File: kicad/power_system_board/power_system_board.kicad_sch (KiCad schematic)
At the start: 0 parts

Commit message: Idea for how we could do charging
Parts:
- added BT1, BT2: Battery_Cell, symbol Device:Battery_Cell
- added C1, C2, C3, C4: 4.7u, symbol Device:C
- added D1, D2: LED, symbol Device:LED
- added J1: USB_B_Micro, symbol Connector:USB_B_Micro
- added R1, R2: 0, symbol Device:R
- added R3, R6: 2k, symbol Device:R
- added R4, R5: 470, symbol Device:R
- added U1, U2: MCP73831-2-OT, Package_TO_SOT_SMD:SOT-23-5, symbol Battery_Management:MCP73831-2-OT
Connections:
- new net: BT2.2 (-), R1.1
- new net: R6.1, U2.5 (PROG)
- new net: BT1.1 (+), R2.2
- new net: R4.1, U1.1 (STAT)
- new net: R3.1, U1.5 (PROG)
- new net: D1.1 (K), R4.2
- new net: R5.1, U2.1 (STAT)
- new net: D2.1 (K), R5.2
- new net +BATT: C1.1, R2.1, U1.3 (V_{BAT})
- new net -BATT: C3.1, C4.2, R1.2, R6.2, U2.2 (V_{SS})
- new net GND: J1.5 (GND)
- new net MID_BATT: BT1.2 (-), BT2.1 (+), C1.2, C2.1, C4.1, R3.2, U1.2 (V_{SS}), U2.3 (V_{BAT})
- new net VBUS: C2.2, C3.2, D1.2 (A), D2.2 (A), J1.1 (VBUS), U1.4 (V_{DD}), U2.4 (V_{DD})
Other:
- note added: "TODO: 1. Battery Charger IC (MCP73831/2 or TP______ something) 2. Undervoltage Lockout 3. Polarity Protection 4. Regulated power rails (5V, 3V3, ..?) 5. Battery health circuit 6. Section for USB input"
- note removed: "TODO: 1. Battery Charger IC (MCP73831/2 or TP______ something) 2. Undervoltage Lockout 3. Polarity Protection 4. Regulated power rails (5V, 3V3, ..?) 5. Battery health circuit"

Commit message: Big headway on the power module
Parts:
- removed R5: 470, symbol Device:R
- removed R6: 2k, symbol Device:R
- C1, C2, C3, C4: footprint (none) -> Capacitor_SMD:C_0805_2012Metric
- D1, D2: footprint (none) -> LED_SMD:LED_0805_2012Metric
- R1: value 0 -> 470; footprint (none) -> Resistor_SMD:R_0805_2012Metric
- R2: value 0 -> 2k
- R4: footprint (none) -> Resistor_SMD:R_0805_2012Metric
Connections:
- net VBUS: now also C2.1, C3.1; no longer C2.2, C3.2
- net at R1.1: now also U2.1 (STAT); no longer BT2.2 (-)
- net at U2.5 (PROG): now also R2.1
- net +BATT1: now reaches BT1.1 (+)
- net +BATT1: now also C1.1, U1.3 (V_{BAT}); no longer R2.2
- net at D2.1 (K): now also R1.2
- removed net +BATT: C1.1, R2.1, U1.3 (V_{BAT})
- net -BATT renamed -BATT2
- net -BATT2: now also BT2.2 (-), C3.2, R2.2; no longer C3.1, R1.2
- net MID_BATT renamed -BATT1
- net -BATT1: now also C2.2; no longer BT2.1 (+), C2.1, C4.1, U2.3 (V_{BAT})
- new net +BATT2: BT2.1 (+), C4.1, U2.3 (V_{BAT})
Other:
- note added: "TODO: (done in brackets) (1.) Battery Charger IC (MCP73831/2 or TP______ something) 2. Undervoltage Lockout 3. Polarity Protection 4. Regulated power rails (5V, 3V3, ..?) 5. Battery health circuit 6. Section for USB input 7. Inline fuse rated at 150% the current of each battery"
- note added: "Unprotected Cells 18650 Cells for now V rated at 3.7V I rated at ????"
- note removed: "TODO: 1. Battery Charger IC (MCP73831/2 or TP______ something) 2. Undervoltage Lockout 3. Polarity Protection 4. Regulated power rails (5V, 3V3, ..?) 5. Battery health circuit 6. Section for USB input"
- moved on the sheet: BT1, C1, D1, J1, R3, R4, U1

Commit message: Its impossible with 2 cells
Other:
- note added: "TODO: (done in brackets) (1.) Battery Charger IC (MCP73831/2 or TP______ something) 2. Undervoltage Lockout 3. Polarity Protection 4. Regulated power rails (JUST 5V) 5. Battery health circuit 6. Section for USB input 7. Inline fuse rated at 150% the current of each battery"
- note removed: "TODO: (done in brackets) (1.) Battery Charger IC (MCP73831/2 or TP______ something) 2. Undervoltage Lockout 3. Polarity Protection 4. Regulated power rails (5V, 3V3, ..?) 5. Battery health circuit 6. Section for USB input 7. Inline fuse rated at 150% the current of each battery"
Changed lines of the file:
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@@
 		)
 	)
-	(text "TODO: (done in brackets)\n(1.) Battery Charger IC (MCP73831/2 or TP______ something)\n2. Undervoltage Lockout\n3. Polarity Protection\n4. Regulated power rails (5V, 3V3, ..?)\n5. Battery health circuit\n6. Section for USB input\n7. Inline fuse rated at 150% the current of each battery\n"
+	(text "TODO: (done in brackets)\n(1.) Battery Charger IC (MCP73831/2 or TP______ something)\n2. Undervoltage Lockout\n3. Polarity Protection\n4. Regulated power rails (JUST 5V)\n5. Battery health circuit\n6. Section for USB input\n7. Inline fuse rated at 150% the current of each battery\n"
 		(exclude_from_sim no)
 		(at 102.362 29.972 0)

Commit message: Nearing end of design
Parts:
- removed BT2: Battery_Cell, symbol Device:Battery_Cell
- removed C4: 4.7u, Capacitor_SMD:C_0805_2012Metric, symbol Device:C
- removed D2: LED, LED_SMD:LED_0805_2012Metric, symbol Device:LED
- removed U2: MCP73831-2-OT, Package_TO_SOT_SMD:SOT-23-5, symbol Battery_Management:MCP73831-2-OT
- added Q1, Q2: 2N7002H, Package_TO_SOT_SMD:SOT-23, symbol Transistor_FET:2N7002H
- added U2: AP9101CK, Package_TO_SOT_SMD:SOT-23-5, symbol Battery_Management:AP9101CK
- C3: value 4.7u -> 100n
- R1: value 470 -> 2k7
- R2: value 2k -> 330; footprint (none) -> Resistor_SMD:R_0805_2012Metric
- R3: footprint (none) -> Resistor_SMD:R_0805_2012Metric
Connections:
- net GND: now also C1.2, C2.2, R1.1, R3.2, U1.2 (V_{SS})
- net VBUS: no longer C3.1
- net at R1.2: now also U2.1 (VM)
- net at R2.1: now also C3.2, U2.2 (VDD)
- net +BATT1 renamed +BATT
- net +BATT: now also R2.2, Q2.2 (S)
- removed net -BATT1: BT1.2 (-), C1.2, C2.2, R3.2, U1.2 (V_{SS})
- removed net -BATT2: C3.2, R2.2
- new net: Q1.1 (G), U2.4 (DO)
- new net: Q1.3 (D), Q2.3 (D)
- new net: Q2.1 (G), U2.5 (CO)
- new net -BATT: BT1.2 (-), C3.1, Q1.2 (S), U2.3 (VSS)
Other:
- note added: "TODO: (done in brackets) (1.) Battery Charger IC (MCP73831/2 or TP______ something) 2. Undervoltage Lockout 3. Polarity Protection 4. Regulated power rails (3V3 - Done on perf board, not on PCB) 5. Battery health circuit 6. Section for USB input 7. Inline fuse rated at 150% the current of each battery"
- note removed: "TODO: (done in brackets) (1.) Battery Charger IC (MCP73831/2 or TP______ something) 2. Undervoltage Lockout 3. Polarity Protection 4. Regulated power rails (JUST 5V) 5. Battery health circuit 6. Section for USB input 7. Inline fuse rated at 150% the current of each battery"
- note removed: "Unprotected Cells 18650 Cells for now V rated at 3.7V I rated at ????"
- moved on the sheet: BT1

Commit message: Checkpoint
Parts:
- removed U2: AP9101CK, Package_TO_SOT_SMD:SOT-23-5, symbol Battery_Management:AP9101CK
- added J2: Conn_01x04_Pin, Connector_PinHeader_2.54mm:PinHeader_1x04_P2.54mm_Vertical, symbol Connector:Conn_01x04_Pin
- added J3, J4, J5, J6: Conn_01x02_Pin, Connector_PinHeader_2.54mm:PinHeader_1x02_P2.54mm_Vertical, symbol Connector:Conn_01x02_Pin
- added R5: 330m, Resistor_SMD:R_0805_2012Metric, symbol Device:R
- added U3: AP9101CK6, Package_TO_SOT_SMD:SOT-23-6, symbol Battery_Management:AP9101CK6
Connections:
- net +BATT: now also J4.1 (Pin_1), J5.2 (Pin_2); no longer BT1.1 (+)
- net -BATT: now also J3.2 (Pin_2), R5.2, U3.6 (VSS); no longer BT1.2 (-), Q1.2 (S)
- net VBUS: now also J2.4 (Pin_4)
- net at J1.2 (D-): now also J2.2 (Pin_2)
- net at J1.3 (D+): now also J2.3 (Pin_3)
- net at J1.4 (ID): now also J2.1 (Pin_1)
- net at Q1.1 (G): now also U3.1 (DO)
- net at Q1.3 (D), Q2.3 (D): now also J5.1 (Pin_1), J6.2 (Pin_2)
- net at Q2.1 (G): now also U3.3 (CO)
- net at R1.2: now also U3.2 (VM)
- net at C3.2, R2.1: now also U3.5 (VDD)
- new net: BT1.1 (+), J4.2 (Pin_2)
- new net: BT1.2 (-), J3.1 (Pin_1)
- new net: J6.1 (Pin_1), Q1.2 (S), R5.1
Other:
- moved on the sheet: BT1, C3, Q1, Q2, R1, R2

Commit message: Checkpoint
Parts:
- added J7: Conn_01x02_Pin, Connector_PinHeader_2.54mm:PinHeader_1x02_P2.54mm_Vertical, symbol Connector:Conn_01x02_Pin
- U3: value AP9101CK6 -> AP9101CK6-AYTRG1
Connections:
- net GND: now also J7.1 (Pin_1)
- net at BT1.2 (-), J3.1 (Pin_1): now also J7.2 (Pin_2)
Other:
- note added: "TODO: (done in brackets) (1.) Battery Charger IC (MCP73831/2 or TP______ something) (2.) Undervoltage Lockout 3. Polarity Protection 4. Regulated power rails (3V3 - Done on perf board, not on PCB) 5. Battery health circuit 6. Section for USB input 7. Inline fuse rated at 150% the current of each battery"
- note removed: "TODO: (done in brackets) (1.) Battery Charger IC (MCP73831/2 or TP______ something) 2. Undervoltage Lockout 3. Polarity Protection 4. Regulated power rails (3V3 - Done on perf board, not on PCB) 5. Battery health circuit 6. Section for USB input 7. Inline fuse rated at 150% the current of each battery"
- moved on the sheet: BT1, J1, J2, J3, J4

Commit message: Need to add esp32 and fix USB
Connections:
- net +BATT: no longer J5.2 (Pin_2), Q2.2 (S)
- net -BATT: now also J6.1 (Pin_1)
- net GND: now also J5.2 (Pin_2), Q2.2 (S)
- net at Q1.2 (S), R5.1: no longer J6.1 (Pin_1)
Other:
- note added: "TODO: (done in brackets) (1.) Battery Charger IC (MCP73831/2 or TP______ something) (2.) Undervoltage Lockout (3.) Polarity Protection (4.) Regulated power rails (3V3 - Done on perf board, not on PCB) 5. Battery health circuit 6. Section for USB input 7. Inline fuse rated at 150% the current of each battery"
- note removed: "TODO: (done in brackets) (1.) Battery Charger IC (MCP73831/2 or TP______ something) (2.) Undervoltage Lockout 3. Polarity Protection 4. Regulated power rails (3V3 - Done on perf board, not on PCB) 5. Battery health circuit 6. Section for USB input 7. Inline fuse rated at 150% the current of each battery"
- moved on the sheet: R5
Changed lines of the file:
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@@
 		(rev "0")
 		(company "University of Cape Town")
-		(comment 1 "Designer: Harry Papanicolaou")
+		(comment 1 "Harry Papanicolaou")
+		(comment 2 "Designers: Adrian McIntosh")
 	)
 	(junction
@@
 	)
 	(junction
-		(at 121.92 62.23)
-		(diameter 0)
-		(color 0 0 0 0)
-	)
-	(junction
 		(at 133.35 77.47)
 		(diameter 0)
@@
 	)
 	(junction
-		(at 133.35 62.23)
+		(at 33.02 35.56)
 		(diameter 0)
 		(color 0 0 0 0)
 	)
 	(junction
-		(at 33.02 35.56)
+		(at 45.72 62.23)
 		(diameter 0)
 		(color 0 0 0 0)
 	)
 	(junction
-		(at 45.72 62.23)
+		(at 83.82 22.86)
 		(diameter 0)
 		(color 0 0 0 0)
 	)
 	(junction
-		(at 63.5 67.31)
+		(at 147.32 91.44)
 		(diameter 0)
 		(color 0 0 0 0)
 	)
 	(junction
-		(at 83.82 22.86)
+		(at 63.5 67.31)
 		(diameter 0)
 		(color 0 0 0 0)
 	)
 	(junction
-		(at 45.72 82.55)
+		(at 133.35 62.23)
 		(diameter 0)
 		(color 0 0 0 0)
 	)
 	(junction
-		(at 133.35 90.17)
+		(at 45.72 82.55)
 		(diameter 0)
 		(color 0 0 0 0)
@@
 	(wire
 		(pts
-			(xy 133.35 88.9) (xy 133.35 90.17)
+			(xy 133.35 88.9) (xy 133.35 91.44)
 		)
 		(stroke
@@
 	(wire
 		(pts
-			(xy 143.51 95.25) (xy 147.32 95.25)
+			(xy 143.51 91.44) (xy 147.32 91.44)
 		)
 		(stroke
@@
 	(wire
 		(pts
-			(xy 133.35 90.17) (xy 133.35 95.25)
+			(xy 133.35 74.93) (xy 133.35 77.47)
 		)
 		(stroke
@@
 	(wire
 		(pts
-			(xy 133.35 74.93) (xy 133.35 77.47)
+			(xy 45.72 60.96) (xy 45.72 62.23)
 		)
 		(stroke
@@
 	(wire
 		(pts
-			(xy 45.72 60.96) (xy 45.72 62.23)
+			(xy 127 58.42) (xy 127 59.69)
 		)
 		(stroke
@@
 	(wire
 		(pts
-			(xy 147.32 86.36) (xy 147.32 90.17)
+			(xy 147.32 86.36) (xy 147.32 91.44)
 		)
 		(stroke
@@
 	(wire
 		(pts
+			(xy 147.32 91.44) (xy 147.32 95.25)
+		)
+		(stroke
+			(width 0)
+			(type default)
+		)
+	)
+	(wire
+		(pts
 			(xy 147.32 72.39) (xy 147.32 77.47)
 		)
@@
 	(wire
 		(pts
-			(xy 133.35 62.23) (xy 121.92 62.23)
-		)
-		(stroke
-			(width 0)
-			(type default)
-		)
-	)
-	(wire
-		(pts
 			(xy 21.59 38.1) (xy 29.21 38.1)
 		)
@@
 	(wire
 		(pts
-			(xy 133.35 95.25) (xy 135.89 95.25)
+			(xy 133.35 91.44) (xy 135.89 91.44)
 		)
 		(stroke
@@
 	(wire
 		(pts
-			(xy 147.32 90.17) (xy 133.35 90.17)
+			(xy 63.5 67.31) (xy 63.5 69.85)
 		)
 		(stroke
@@
 	(wire
 		(pts
-			(xy 63.5 67.31) (xy 63.5 69.85)
+			(xy 133.35 58.42) (xy 127 58.42)
 		)
 		(stroke
@@
 	(wire
 		(pts
+			(xy 133.35 62.23) (xy 133.35 58.42)
+		)
+		(stroke
+			(width 0)
+			(type default)
+		)
+	)
+	(wire
+		(pts
 			(xy 115.57 80.01) (xy 120.65 80.01)
 		)
@@
 	(rectangle
 		(start 77.47 52.07)
-		(end 179.07 125.73)
+		(end 173.99 125.73)
 		(stroke
 			(width 0)
@@
 	(rectangle
 		(start 12.7 52.07)
-		(end 76.2 125.73)
+		(end 76.2 116.84)
 		(stroke
 			(width 0)
@@
 	)
 	(image
-		(at 33.02 106.68)
+		(at 33.02 104.14)
 		(scale 0.158222)
 		(data "iVBORw0KGgoAAAANSUhEUgAAA3sAAAIfCAYAAADJ38UbAAAAAXNSR0IArs4c6QAAAARnQU1BAACx"
@@
 		)
 	)
-	(text_box "AP9101C\n1) Protects from overdischarge (UVLO)\n2) Selectable power-down mode. We don't need this\n\n<< This is a reference, but because of the charging circuit, P- and GND are swapped\nI saw a video on youtube saying that a small resister where R5 is would make it smoother"
+	(text_box "AP9101C battery protection circuit with failsafes\n1) Protects from overdischarge (UVLO)\n2) Selectable power-down mode. We don't need this\n3) Overdischarge also works as polarity protection :)\n\n<< This is a reference, but because of the charging circuit, P- and GND are swapped\nI saw a video on youtube saying that a small resister where R5 is would make it smoother"
 		(exclude_from_sim no)
 		(at 116.84 101.6 0)
-		(size 44.45 21.59)
+		(size 55.88 22.86)
 		(stroke
 			(width 0)
@@
 	(text_box "Battery Charging IC modules\nEach cell is disconnected and charged seperately from one another"
 		(exclude_from_sim no)
-		(at 52.07 100.33 0)
+		(at 52.07 97.79 0)
 		(size 22.86 17.78)
 		(stroke
@@
 		)
 	)
-	(text "TODO: (done in brackets)\n(1.) Battery Charger IC (MCP73831/2 or TP______ something)\n(2.) Undervoltage Lockout\n3. Polarity Protection\n4. Regulated power rails (3V3 - Done on perf board, not on PCB)\n5. Battery health circuit\n6. Section for USB input\n7. Inline fuse rated at 150% the current of each battery\n"
+	(text "TODO: (done in brackets)\n(1.) Battery Charger IC (MCP73831/2 or TP______ something)\n(2.) Undervoltage Lockout\n(3.) Polarity Protection\n(4.) Regulated power rails (3V3 - Done on perf board, not on PCB)\n5. Battery health circuit\n6. Section for USB input\n7. Inline fuse rated at 150% the current of each battery\n"
 		(exclude_from_sim no)
 		(at 117.602 30.734 0)
@@
 	)
 	(symbol
+		(lib_id "power:GND")
+		(at 127 59.69 0)
+		(unit 1)
+		(exclude_from_sim no)
+		(in_bom yes)
+		(on_board yes)
+		(dnp no)
+		(fields_autoplaced yes)
+		(property "Reference" "#PWR016"
+			(at 127 66.04 0)
+			(effects
+				(font
+					(size 1.27 1.27)
+				)
+				(hide yes)
+			)
+		)
+		(property "Value" "GND"
+			(at 127 64.77 0)
+			(effects
+				(font
+					(size 1.27 1.27)
+				)
+			)
+		)
+		(property "Footprint" ""
+			(at 127 59.69 0)
+			(effects
+				(font
+					(size 1.27 1.27)
+				)
+				(hide yes)
+			)
+		)
+		(property "Datasheet" ""
+			(at 127 59.69 0)
+			(effects
+				(font
+					(size 1.27 1.27)
+				)
+				(hide yes)
+			)
+		)
+		(property "Description" "Power symbol creates a global label with name \"GND\" , ground"
+			(at 127 59.69 0)
+			(effects
+				(font
+					(size 1.27 1.27)
+				)
+				(hide yes)
+			)
+		)
+		(pin "1"
+		)
+		(instances
+			(project "power_system_board"
+				(path "/1f2c619c-07aa-42fb-b852-c9242f165a43"
+					(reference "#PWR016")
+					(unit 1)
+				)
+			)
+		)
+	)
+	(symbol
 		(lib_id "power:VBUS")
 		(at 45.72 60.96 0)
@@
 	(symbol
 		(lib_id "Device:R")
-		(at 139.7 95.25 90)
+		(at 139.7 91.44 90)
 		(unit 1)
 		(exclude_from_sim no)
@@
 		(dnp no)
 		(property "Reference" "R5"
-			(at 139.7 99.822 90)
+			(at 139.7 96.012 90)
 			(effects
 				(font
@@
 		)
 		(property "Value" "330m"
-			(at 139.7 97.536 90)
+			(at 139.7 93.726 90)
 			(effects
 				(font
@@
 		)
 		(property "Footprint" "Resistor_SMD:R_0805_2012Metric"
-			(at 139.7 97.028 90)
+			(at 139.7 93.218 90)
 			(effects
 				(font
@@
 		)
 		(property "Datasheet" "~"
-			(at 139.7 95.25 0)
+			(at 139.7 91.44 0)
 			(effects
 				(font
@@
 		)
 		(property "Description" "Resistor"
-			(at 139.7 95.25 0)
+			(at 139.7 91.44 0)
 			(effects
 				(font

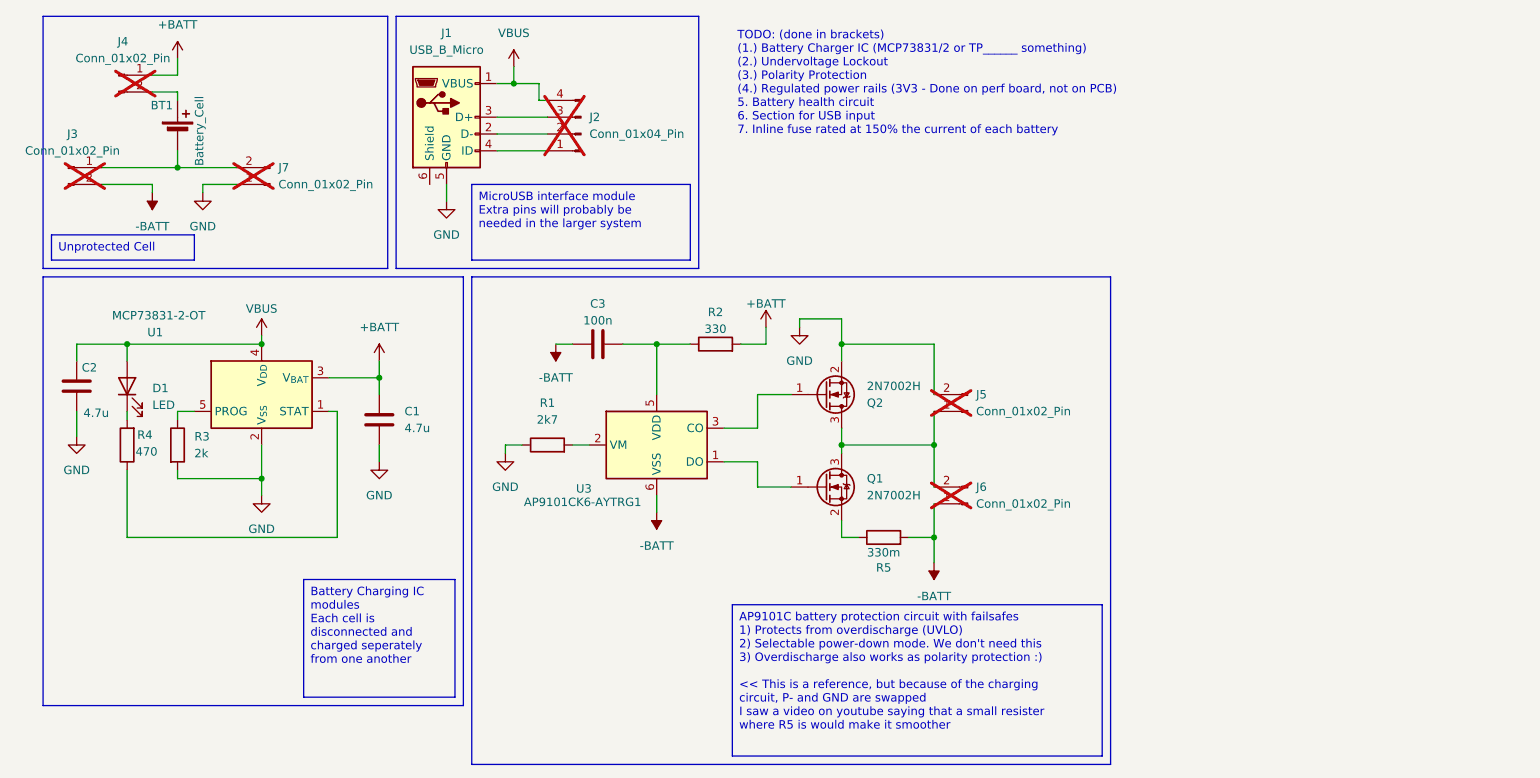
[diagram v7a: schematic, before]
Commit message: Need to add esp32 and fix USB latest => 7:42
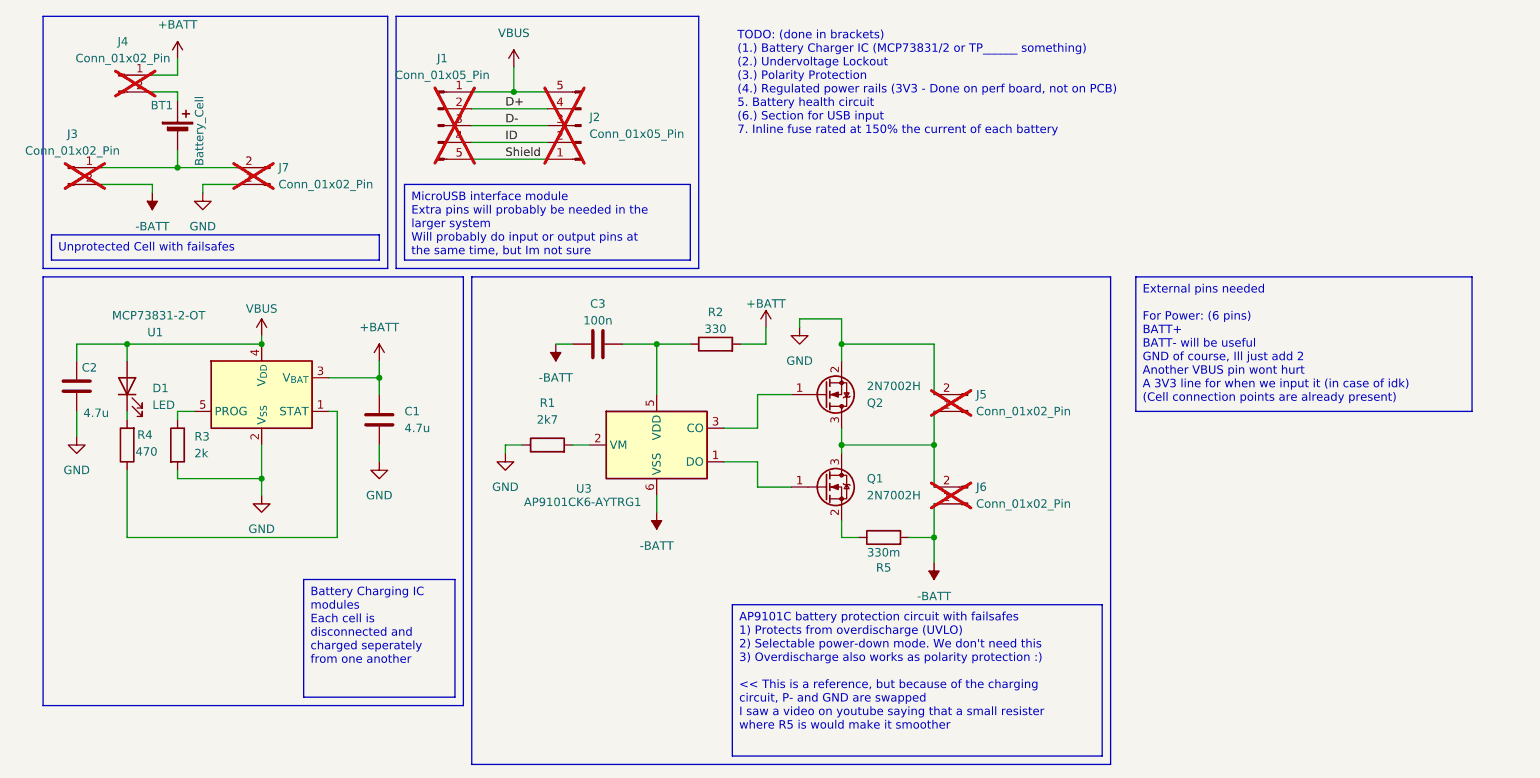
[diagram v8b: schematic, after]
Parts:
- removed J1: USB_B_Micro, symbol Connector:USB_B_Micro
- removed J2: Conn_01x04_Pin, Connector_PinHeader_2.54mm:PinHeader_1x04_P2.54mm_Vertical, symbol Connector:Conn_01x04_Pin
- added J1, J2: Conn_01x05_Pin, Connector_PinHeader_2.54mm:PinHeader_1x05_P2.54mm_Vertical, symbol Connector:Conn_01x05_Pin
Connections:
- net VBUS: now also J1.1 (Pin_1), J2.5 (Pin_5)
- new net D+: J1.2 (Pin_2), J2.4 (Pin_4)
- new net D-: J1.3 (Pin_3), J2.3 (Pin_3)
- new net ID: J1.4 (Pin_4), J2.2 (Pin_2)
- new net Shield: J1.5 (Pin_5), J2.1 (Pin_1)
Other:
- note added: "TODO: (done in brackets) (1.) Battery Charger IC (MCP73831/2 or TP______ something) (2.) Undervoltage Lockout (3.) Polarity Protection (4.) Regulated power rails (3V3 - Done on perf board, not on PCB) 5. Battery health circuit (6.) Section for USB input 7. Inline fuse rated at 150% the current of each battery"
- note removed: "TODO: (done in brackets) (1.) Battery Charger IC (MCP73831/2 or TP______ something) (2.) Undervoltage Lockout (3.) Polarity Protection (4.) Regulated power rails (3V3 - Done on perf board, not on PCB) 5. Battery health circuit 6. Section for USB input 7. Inline fuse rated at 150% the current of each battery"
